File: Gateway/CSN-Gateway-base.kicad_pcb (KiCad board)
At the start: 2 copper layers, 32 x 85.5 mm, 56 parts, among them IC1 ATMEGA328-A, P1 CONN_02X06, P2 CONN4, P3 CONN_ICSP, P5 CONN6, Q1 2N2222, U1 MAX485CSA, U2 AMS1117-3.3V, U3 ATSHA204A, Y1 Crystal

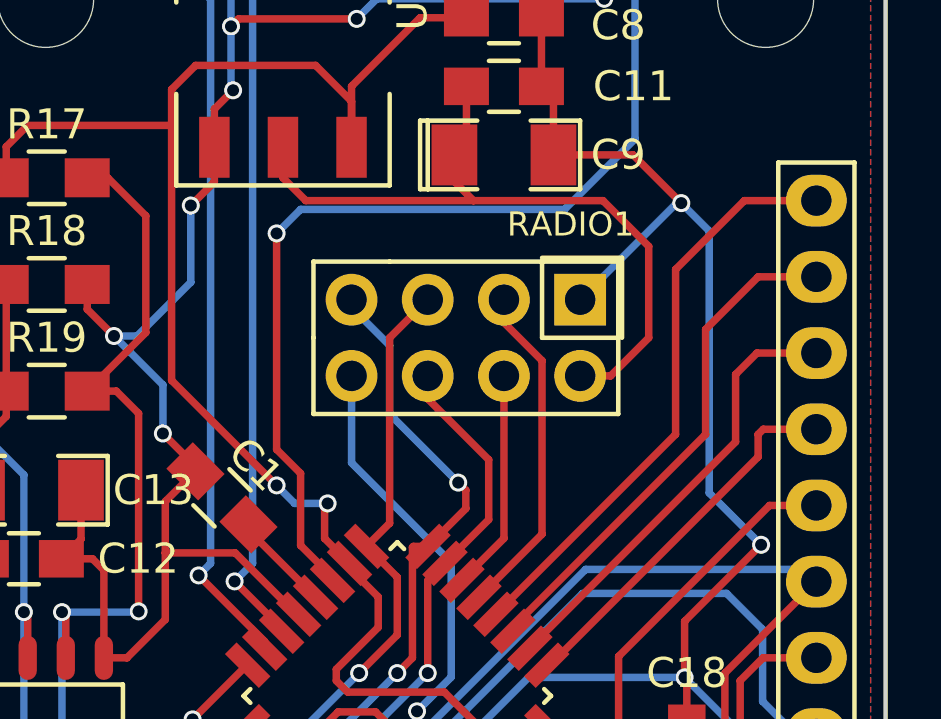
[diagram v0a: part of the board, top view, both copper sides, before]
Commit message: add silkscreen infos on pcb
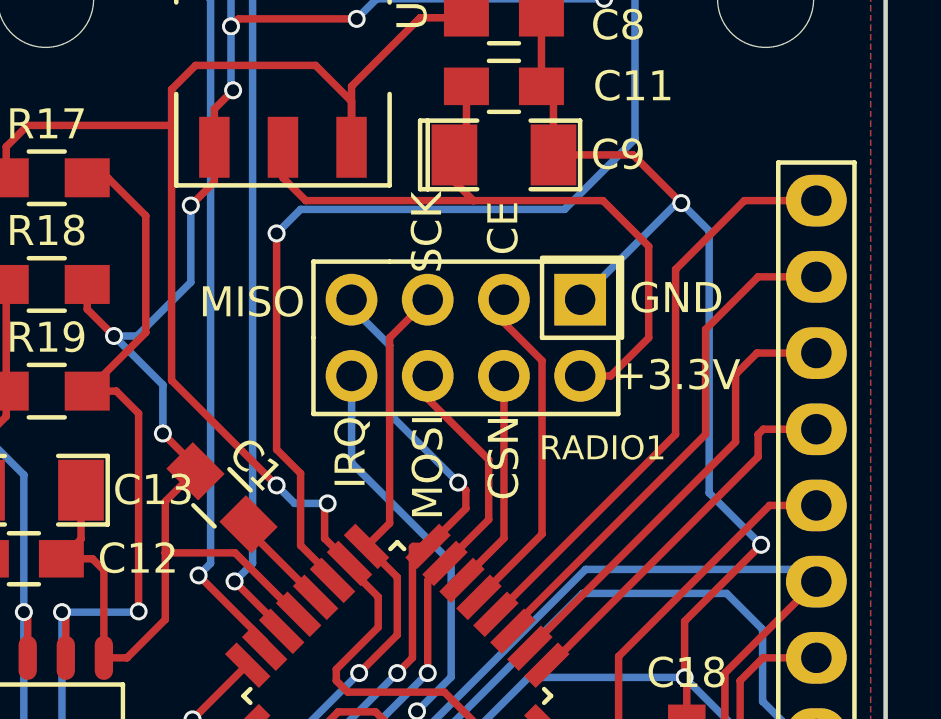
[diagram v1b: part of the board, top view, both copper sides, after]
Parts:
- added G***: LOGO, libs:calaos_logo, B.Cu at (119.9, 93.3)
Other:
- board text added: "+3.3V"
- board text added: "+5V +24V"
- board text added: "A"
- board text added: "B"
- board text added: "BTN1"
- board text added: "BTN2"
- board text added: "CE"
- board text added: "CSN"
- board text added: "CT Sensor 0"
- board text added: "CT Sensor 1"
- board text added: "CT Sensor 2"
- board text added: "CT Sensor 3"
- board text added: "GND"
- board text added: "Gateway v1.0"
- board text added: "IRQ"
- board text added: "MISO"
- board text added: "MOSI"
- board text added: "Power"
- board text added: "RGB1"
- board text added: "RGB2"
- board text added: "RGB3"
- board text added: "RS485"
- board text added: "RST"
- board text added: "RXI"
- board text added: "SCK"
- board text added: "SCL"
- board text added: "SDA"
- board text added: "TXO"
- board text added: "VCC"

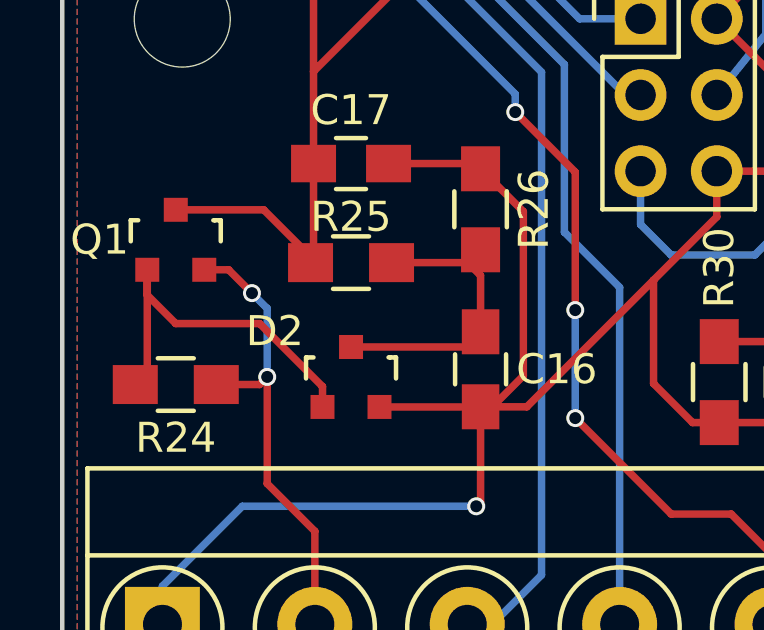
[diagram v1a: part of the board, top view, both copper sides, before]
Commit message: fix wrong footprints
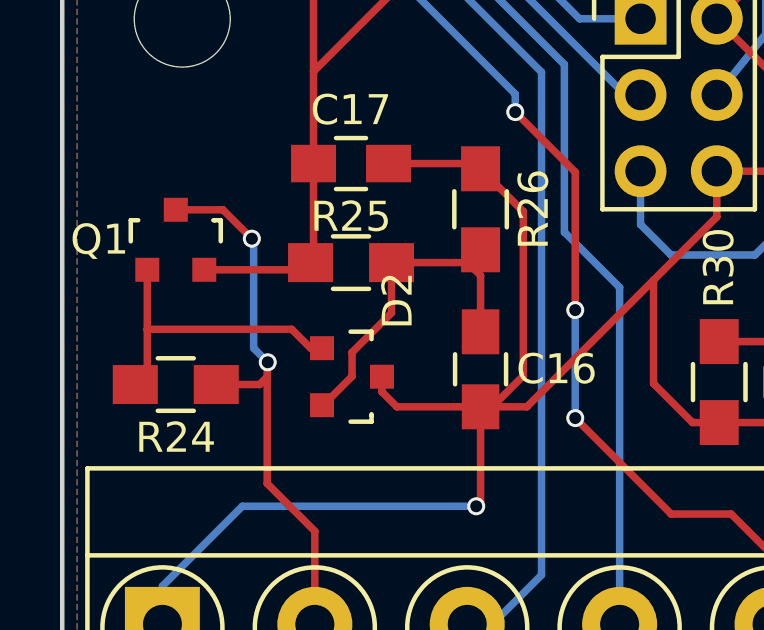
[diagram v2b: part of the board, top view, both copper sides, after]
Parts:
- turned D2 to 270 degrees
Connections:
- C10 pad 2: GND -> Net-(C10-Pad2)
- C11 pad 2: GND -> Net-(C10-Pad2)
- C8 pad 1: GND -> Net-(C10-Pad2)
- C9 pad 2: GND -> Net-(C10-Pad2)
- D2 pad 2: GND -> Net-(C16-Pad1)
- D2 pad 3: Net-(C16-Pad1) -> GND
- Q1 pad 2: Net-(P2-Pad2) -> VCC
- Q1 pad 3: VCC -> Net-(P2-Pad2)
- U2 pad 1: GND -> Net-(C10-Pad2)
- U2 pad 4: GND -> (no net)
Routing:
- net Net-(C10-Pad2): track 0.00 -> 51.0 mm, vias 0 -> 5
- net GND: track 257.6 -> 207.2 mm, vias 20 -> 15
- net Net-(P2-Pad2): track 15.6 -> 18.5 mm
- net Net-(D2-Pad1): track 12.6 -> 10.1 mm
- net Net-(C16-Pad1): track 9.55 -> 11.5 mm
- net VCC: track 219.0 -> 217.4 mm

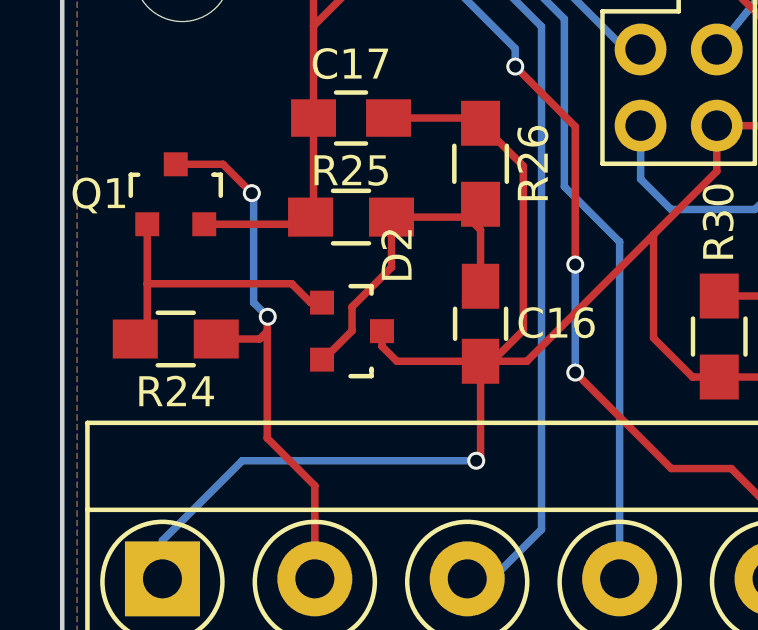
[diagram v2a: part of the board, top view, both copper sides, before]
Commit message: Fix footprints for power supply components
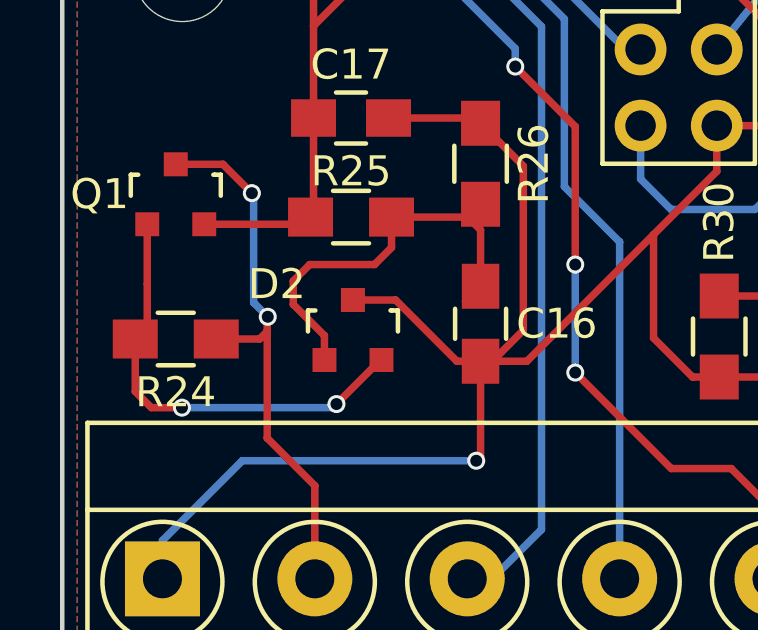
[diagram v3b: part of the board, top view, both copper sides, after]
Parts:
- moved D2 0.05 mm to (119.2, 122.4), turned to 0 degrees
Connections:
- C10 pad 2: Net-(C10-Pad2) -> GND
- C11 pad 2: Net-(C10-Pad2) -> GND
- C8 pad 1: Net-(C10-Pad2) -> GND
- C9 pad 2: Net-(C10-Pad2) -> GND
- D2 pad 1: Net-(D2-Pad1) -> Net-(C16-Pad1)
- D2 pad 2: Net-(C16-Pad1) -> Net-(D2-Pad2)
- Q1 pad 1: Net-(D2-Pad1) -> Net-(D2-Pad2)
- R24 pad 2: Net-(D2-Pad1) -> Net-(D2-Pad2)
- U2 pad 1: Net-(C10-Pad2) -> GND
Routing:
- net GND: track 207.2 -> 259.3 mm, vias 15 -> 20
- net Net-(C10-Pad2): track 51.0 -> 0.00 mm, vias 5 -> 0
- net Net-(D2-Pad2): track 0.00 -> 14.8 mm, vias 0 -> 2
- net Net-(D2-Pad1): track 10.1 -> 0.00 mm
- net Net-(C16-Pad1): track 11.5 -> 13.6 mm

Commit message: new pcb for v1.1 prototype
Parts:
- added C2: 0.1uF, Capacitors_SMD:C_0805_HandSoldering, B.Cu at (123.3, 109.7)
- C10, C13, C9: footprint SMD_Packages:SMD-1206_Pol -> Capacitors_Tantalum_SMD:CP_Tantalum_Case-R_EIA-2012-12_Hand
- C11, C8: moved to B.Cu
- C17, C20, C5, C6, C7: footprint Capacitors_SMD:C_0805_HandSoldering -> Capacitors_Tantalum_SMD:CP_Tantalum_Case-R_EIA-2012-12_Hand
- P1: footprint Socket_Strips:Socket_Strip_Straight_1x12 -> Connectors:IDC_Header_Straight_12pins
- P3: footprint Pin_Headers:Pin_Header_Straight_2x03 -> Pin_Headers:Pin_Header_Straight_2x03_Pitch2.54mm
- Y1: footprint mysensors_obscurities:XTAL_3.2x1.5mm -> Crystals:Crystal_SMD_5032-2pin_5.0x3.2mm
- moved U3 20.3 mm to (136.7, 79.5)
- moved C18 20.1 mm to (136.4, 75.4), turned to 180 degrees
- moved P1 16.3 mm to (134.9, 88.9), turned to 270 degrees
- moved C14 8.98 mm to (119.6, 98.3), turned to 315 degrees
- moved R1 6.83 mm to (119.6, 109.7)
- moved C10 3.57 mm to (128.8, 71.9)
- moved Y1 3.09 mm to (123.7, 105.2)
- moved R4 2.79 mm to (137.2, 63.8)
- moved C5 2.55 mm to (134.4, 64.0)
- moved C1 2.40 mm to (120.7, 84.6)
- moved C11 2.03 mm to (128.8, 70.9)
- moved C8 2.03 mm to (128.8, 68.6)
- moved C3 1.70 mm to (128.8, 106.9)
- moved C20 1.70 mm to (132.6, 121.4)
- moved C4 1.55 mm to (128.8, 103.4)
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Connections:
- IC1 pad 29: RST -> Net-(C2-Pad1)
- R1 pad 2: RST -> Net-(C2-Pad1)
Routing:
- net GND: track 259.3 -> 224.0 mm, vias 20 -> 9
- net RGB2: track 17.2 -> 47.2 mm, vias 0 -> 4
- net RST: track 62.4 -> 38.4 mm, vias 2 -> 4
- net Net-(C2-Pad1): track 0.00 -> 19.2 mm, vias 0 -> 3
- net BTN2: track 15.0 -> 33.2 mm, vias 0 -> 5
- net Net-(C3-Pad1): track 16.3 -> 33.8 mm, vias 2 -> 4
- net BTN1: track 20.1 -> 30.2 mm
- net A3: track 55.2 -> 65.3 mm, vias 6 -> 3
- net SDA: track 35.1 -> 43.9 mm, vias 1 -> 3
- net RS485-A: track 68.6 -> 61.0 mm, vias 2 -> 5
- net RGB1: track 19.6 -> 26.6 mm, vias 0 -> 1
- net Net-(C11-Pad1): track 24.8 -> 18.4 mm, vias 0 -> 3
- net Net-(C6-Pad1): track 27.5 -> 21.1 mm, vias 1 -> 0
- net A1: track 46.5 -> 40.6 mm, vias 1 -> 4
- net RXI: track 21.7 -> 27.5 mm
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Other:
- board text added: "Gateway v1.1"
- board text removed: "BTN1"
- board text removed: "BTN2"
- board text removed: "Gateway v1.0"
- board text removed: "RGB1"
- board text removed: "RGB2"
- board text removed: "RGB3"
- board text removed: "RXI"
- board text removed: "SCL"
- board text removed: "SDA"
- board text removed: "TXO"

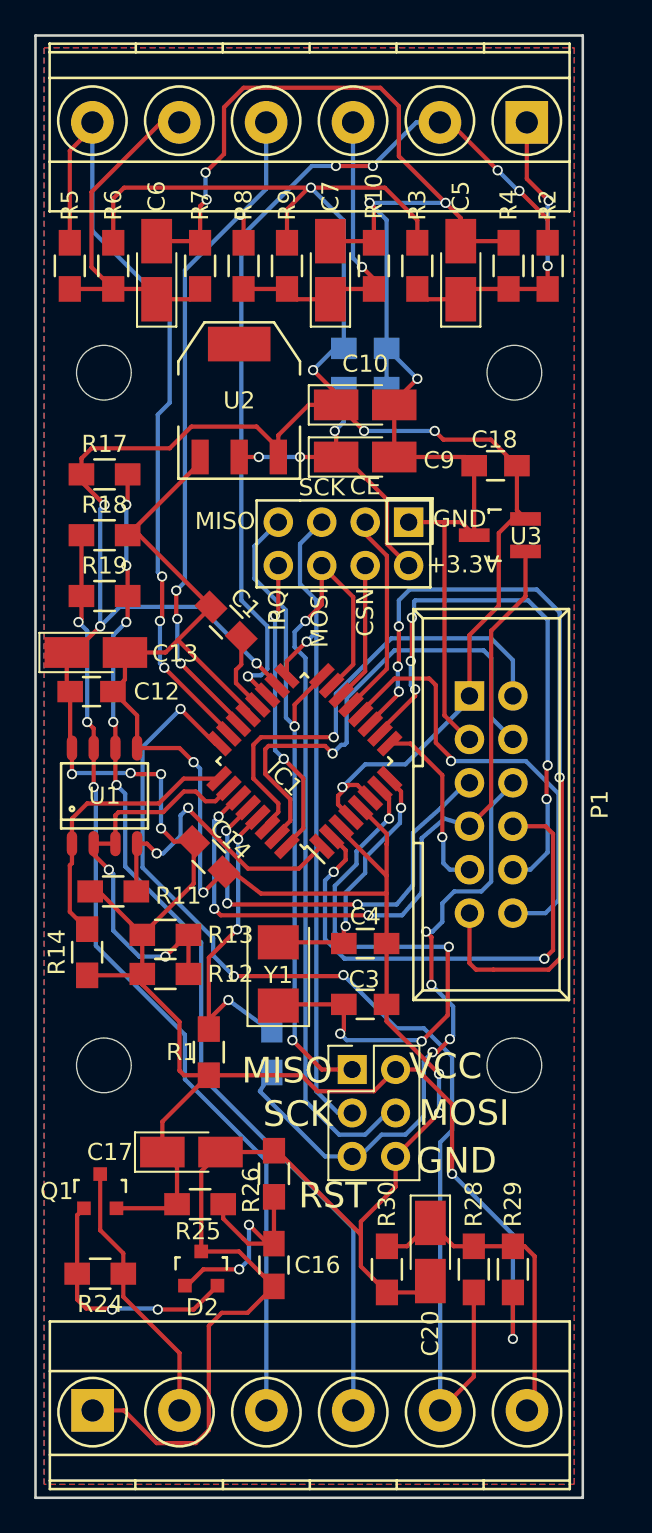
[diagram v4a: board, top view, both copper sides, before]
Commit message: 4 layers version of the base pcb
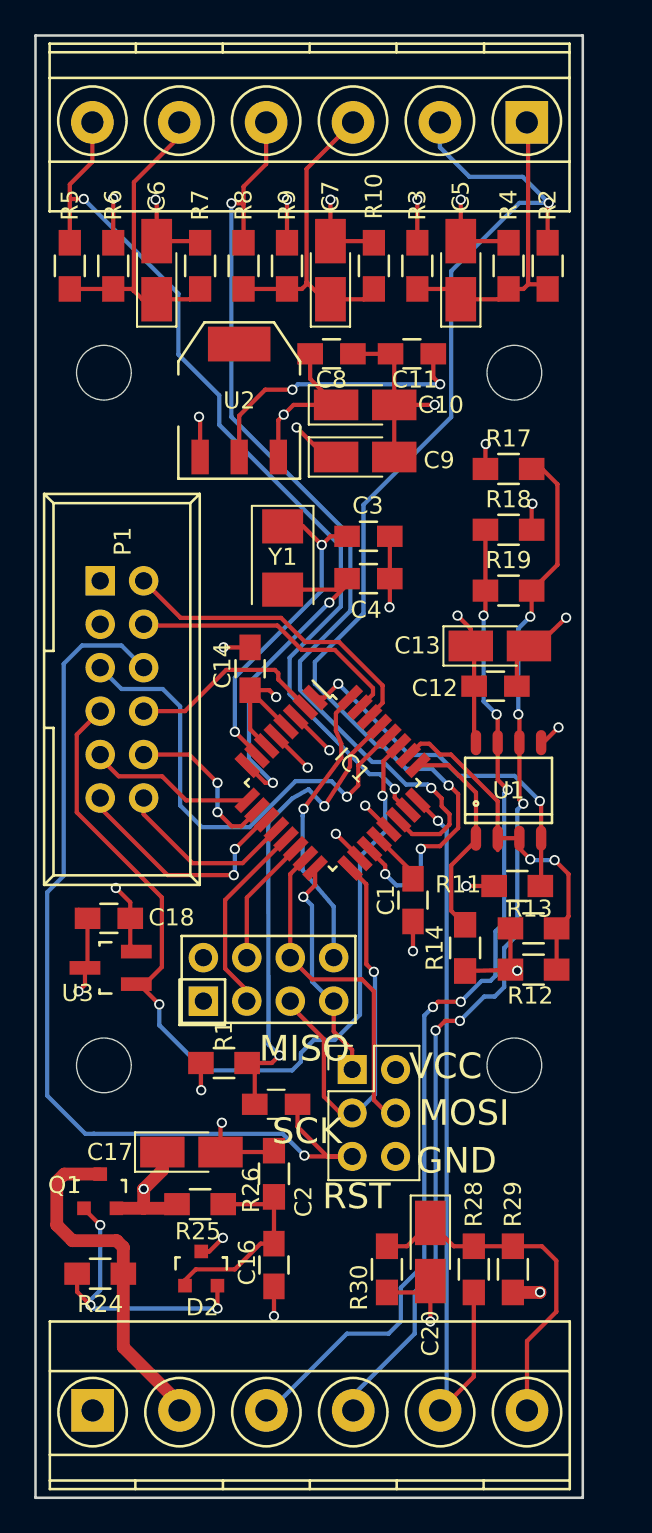
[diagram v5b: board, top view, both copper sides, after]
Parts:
- C11, C2, C8: moved to F.Cu
- moved C18 34.8 mm to (113.8, 101.9)
- moved RADIO1 34.5 mm to (117.8, 108.3), turned to 180 degrees
- moved U3 34.0 mm to (113.9, 104.8)
- moved C3 27.4 mm to (129.0, 79.6)
- moved Y1 24.3 mm to (124.0, 80.8), turned to 270 degrees
- moved C13 23.6 mm to (136.7, 86.0)
- moved C12 23.6 mm to (136.4, 88.3)
- moved R11 23.6 mm to (137.7, 100.0)
- moved R17 23.6 mm to (137.2, 75.6)
- moved R18 23.6 mm to (137.2, 79.2)
- moved R19 23.6 mm to (137.2, 82.7)
- moved U1 23.6 mm to (137.2, 94.4)
- moved P1 22.6 mm to (113.3, 82.2)
- moved R14 22.1 mm to (134.6, 103.6)
- moved R13 21.5 mm to (138.6, 102.5)
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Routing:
- net VCC: track 217.2 -> 60.6 mm
- net GND: track 224.0 -> 70.3 mm, vias 9 -> 19
- net Net-(C11-Pad1): track 18.4 -> 58.6 mm
- net RGB2: track 47.2 -> 14.1 mm, vias 4 -> 2
- net MOSI: track 47.2 -> 19.8 mm, vias 1 -> 0
- net MISO: track 39.7 -> 13.3 mm, vias 2 -> 1
- net BTN2: track 33.2 -> 9.78 mm, vias 5 -> 2
- net A3: track 65.3 -> 44.2 mm, vias 3 -> 1
- net BTN1: track 30.2 -> 11.6 mm, vias 2 -> 0
- net RST: track 38.4 -> 55.9 mm, vias 4 -> 1
- net A1: track 40.6 -> 57.5 mm, vias 4 -> 2
- net SCK: track 40.0 -> 24.1 mm
- net RGB1: track 26.6 -> 10.7 mm, vias 1 -> 0
- net A0: track 53.2 -> 68.2 mm, vias 5 -> 4
- net Net-(C3-Pad1): track 33.8 -> 19.5 mm, vias 4 -> 2
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- added copper zone on Ground.Plane, net GND
- added copper zone on Power.Plane, net VCC
- removed copper zone on B.Cu, net GND
- removed copper zone on F.Cu, net GND
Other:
- copper layers 2 -> 4
- net class Power added: clearance 0.2, trace_width 0.75, via_dia 0.6, via_drill 0.4
- board text added: "Gateway v1.2"
- board text removed: "+3.3V"
- board text removed: "CE"
- board text removed: "CSN"
- board text removed: "Gateway v1.1"
- board text removed: "IRQ"

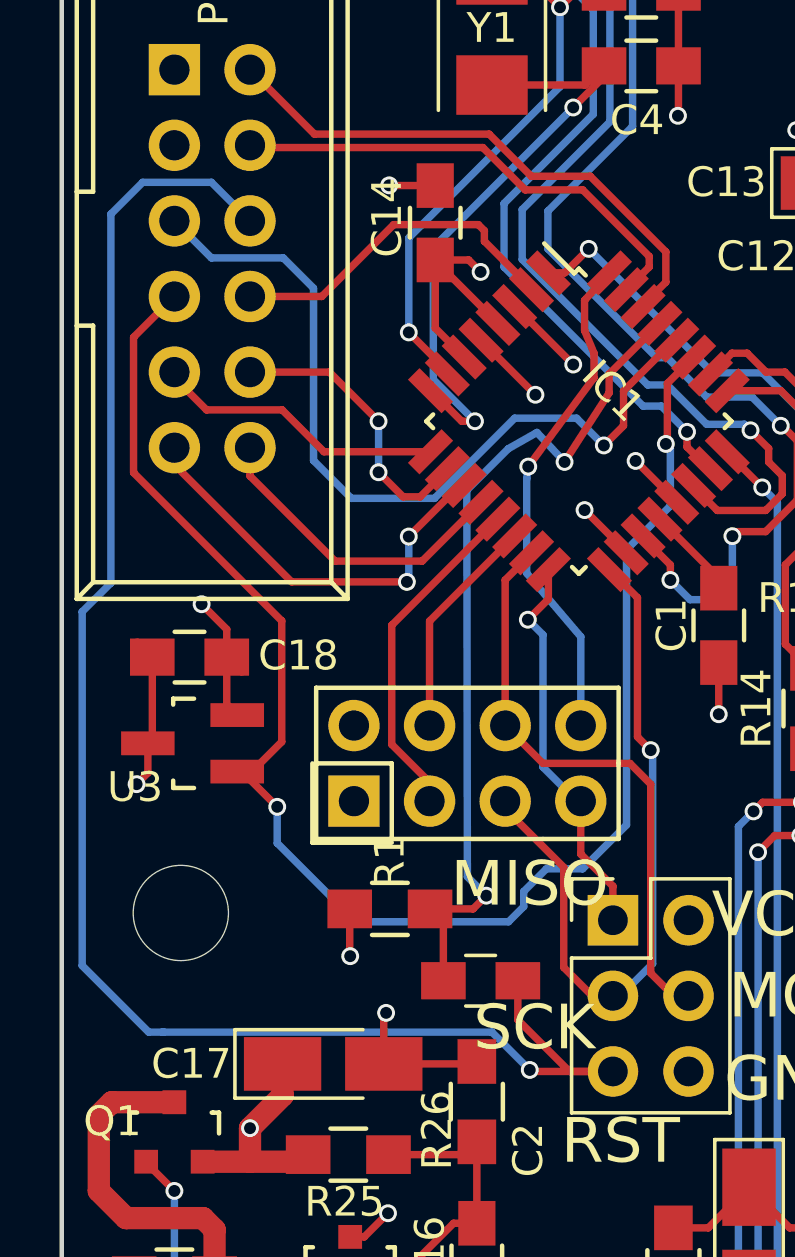
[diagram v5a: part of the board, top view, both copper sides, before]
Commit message: Fix wrong reset pin for ICSP, fix exchange of rx/tx in ftdi
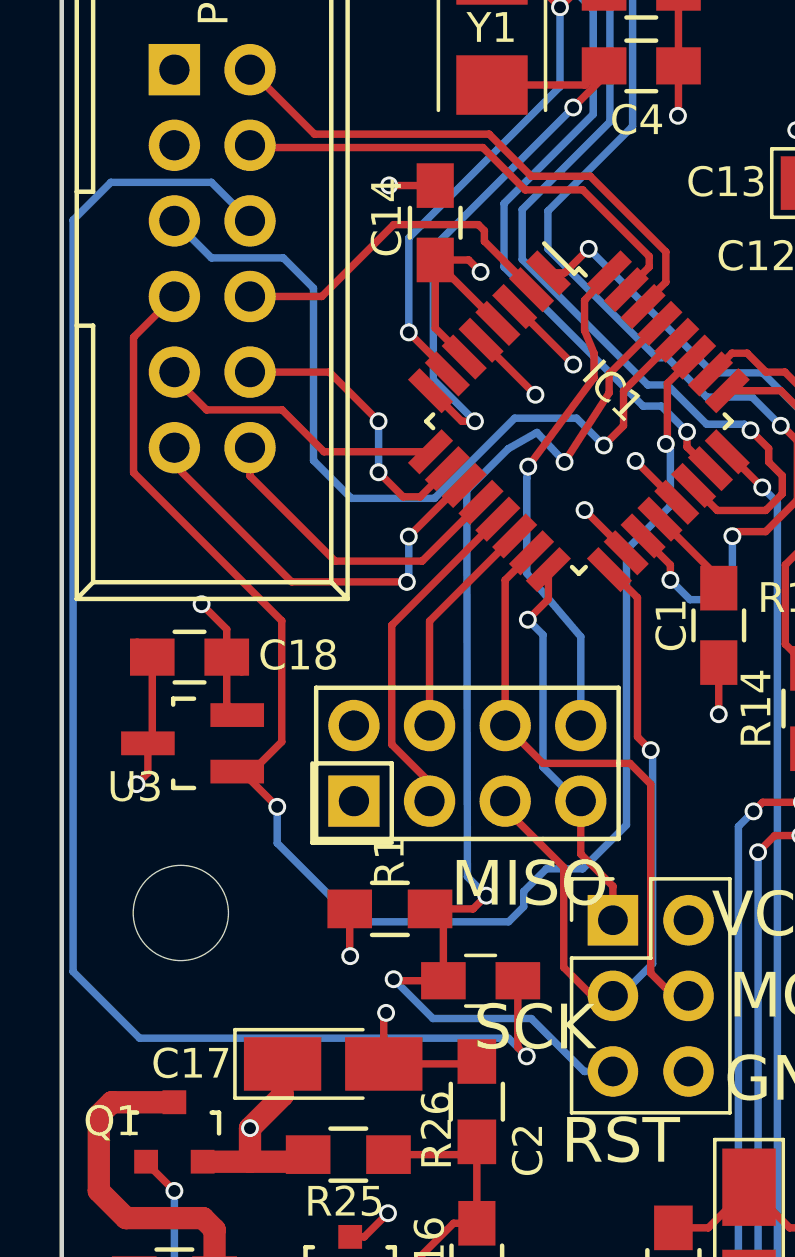
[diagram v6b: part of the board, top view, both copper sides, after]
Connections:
- C2 pad 1: Net-(C2-Pad1) -> RRST
- IC1 pad 29: Net-(C2-Pad1) -> RRST
- P3 pad 5: RST -> RRST
- R1 pad 2: Net-(C2-Pad1) -> RRST
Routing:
- net RRST: track 0.00 -> 39.1 mm, vias 0 -> 3
- net Net-(C2-Pad1): track 28.8 -> 0.00 mm, vias 2 -> 0
- net RST: track 55.9 -> 51.3 mm
